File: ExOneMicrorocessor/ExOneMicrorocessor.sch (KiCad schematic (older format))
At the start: 15 parts, among them IC1 STM32G041C8T6, IC2 FT230XS, IC3 TLV73333PQDBVRQ1, J1 UJ2-MBH-3-SMT, J2 Conn_01x02, Y1 32.768 kHz, Y2 8 MHz

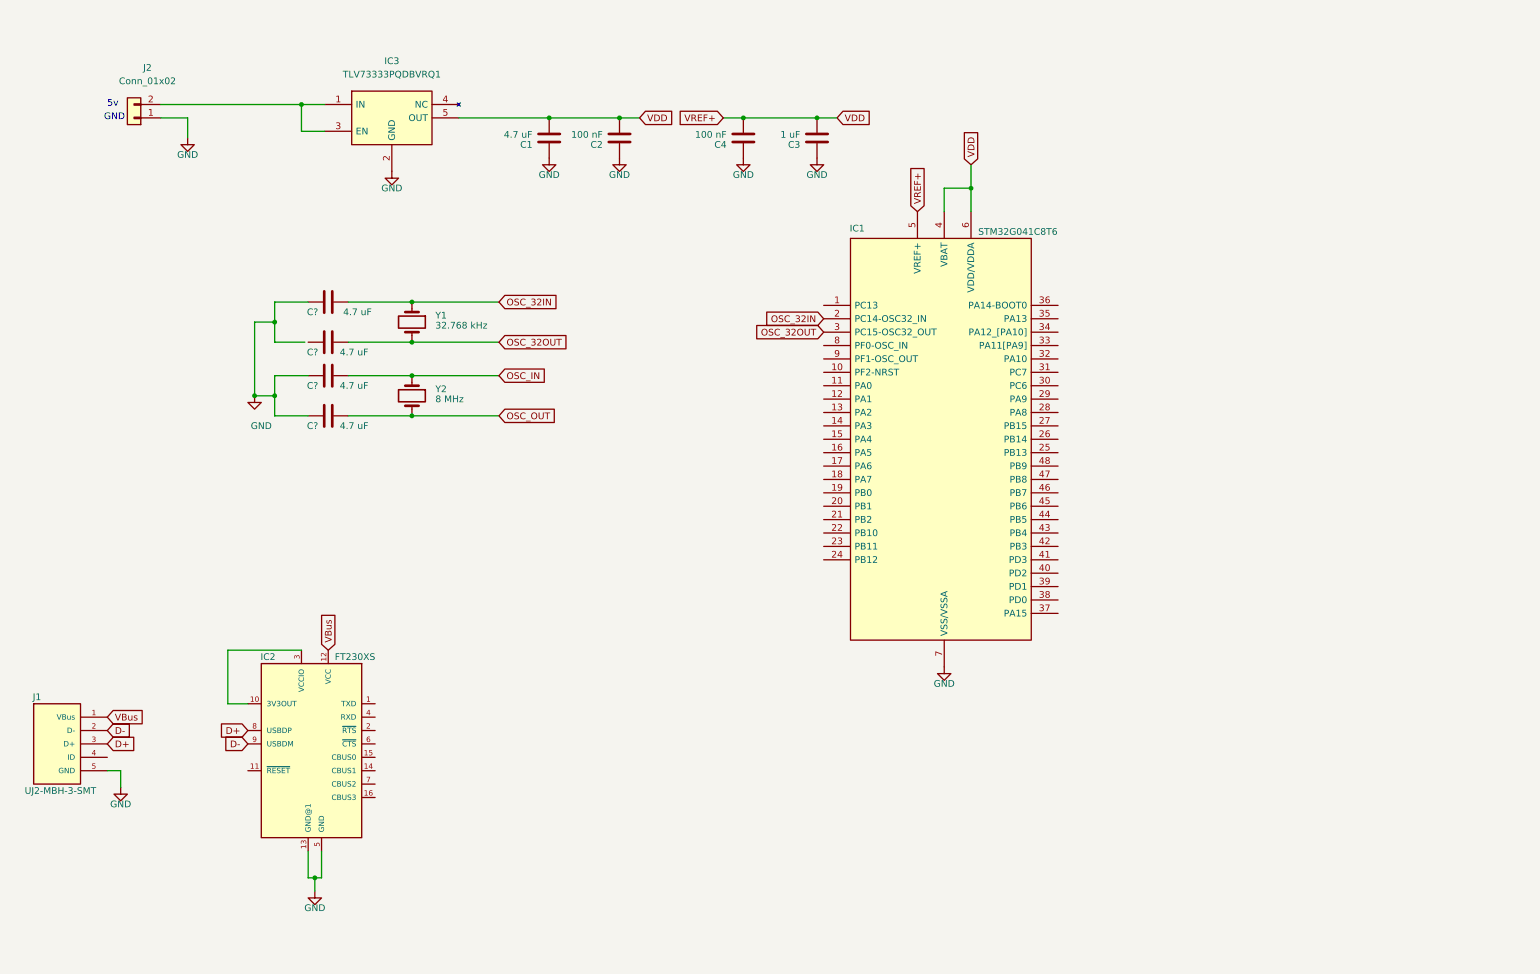
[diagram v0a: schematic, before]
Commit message: finished the schematic for the microP
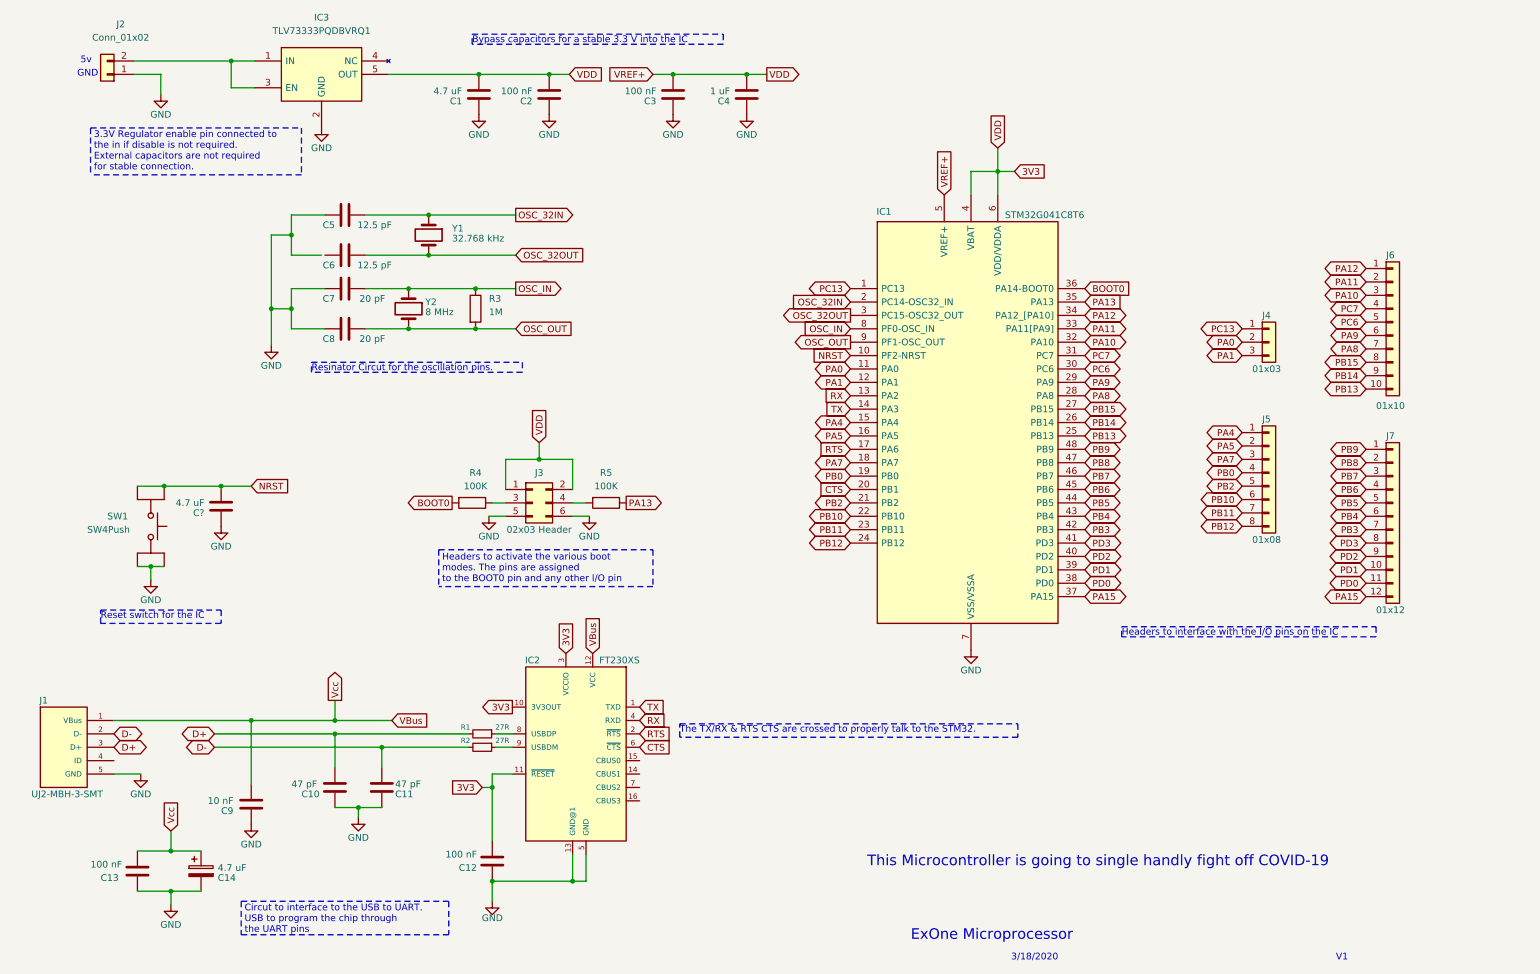
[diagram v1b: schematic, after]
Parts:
- added C10, C11: 47 pF, symbol Device:C
- added C12, C13: 100 nF, symbol Device:C
- added C14: 4.7 uF, symbol Device:CP
- added C9: 10 nF, symbol Device:C
- added C?: 4.7 uF, symbol Device:C
- added J3: 02x03 Header, symbol Connector_Generic:Conn_02x03_Odd_Even
- added J4: 01x03, symbol Connector_Generic:Conn_01x03
- added J5: 01x08, symbol Connector_Generic:Conn_01x08
- added J6: 01x10, symbol Connector_Generic:Conn_01x10
- added J7: 01x12, symbol Connector_Generic:Conn_01x12
- added R1, R2: 27R, symbol Device:R_Small
- added R3: 1M, symbol Device:R
- added R4, R5: 100K, symbol Device:R
- added SW1: SW4Push, symbol Switch4Prong:SW4Push
- C5, C6: renamed from C?; value 4.7 uF -> 12.5 pF
- C7, C8: renamed from C?; value 4.7 uF -> 20 pF
- renumbered C4 to C3, C3 to C4
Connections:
- net VDD is gone; now on net 3V3: C1.2, C2.2, C3.2, C4.2, IC1.4 (VBAT), IC1.5 (VREF+), IC1.6 (VDD/VDDA), IC3.5 (OUT)
- net D+: now also C10.1, R1.2; no longer IC2.8 (USBDP)
- net D-: now also C11.1, R2.2; no longer IC2.9 (USBDM)
- net GND: now also C10.2, C11.2, C12.2, C13.2, C14.2, C9.2, C?.1, J3.5 (Pin_5), J3.6 (Pin_6), SW1.1, SW1.4
- net OSC_IN: now also IC1.8 (PF0-OSC_IN), R3.1
- net OSC_OUT: now also IC1.9 (PF1-OSC_OUT), R3.2
- net VBus: now also C13.1, C14.1, C9.1
- net PC13: now reaches IC1.1 (PC13)
- net PC13: now also J4.1 (Pin_1)
- net NRST: now reaches IC1.10 (PF2-NRST)
- net NRST: now also C?.2, SW1.2, SW1.3
- net PA0: now reaches IC1.11 (PA0)
- net PA0: now also J4.2 (Pin_2)
- net PA1: now reaches IC1.12 (PA1)
- net PA1: now also J4.3 (Pin_3)
- net RX: now reaches IC1.13 (PA2)
- net RX: now also IC2.4 (RXD)
- net TX: now reaches IC1.14 (PA3)
- net TX: now also IC2.1 (TXD)
- net PA4: now reaches IC1.15 (PA4)
- net PA4: now also J5.1 (Pin_1)
- net PA5: now reaches IC1.16 (PA5)
- net PA5: now also J5.2 (Pin_2)
- net RTS: now reaches IC1.17 (PA6)
- net RTS: now also IC2.2 (~RTS~)
- net PA7: now reaches IC1.18 (PA7)
- net PA7: now also J5.3 (Pin_3)
- net PB0: now reaches IC1.19 (PB0)
- net PB0: now also J5.4 (Pin_4)
- net CTS: now reaches IC1.20 (PB1)
- net CTS: now also IC2.6 (~CTS~)
- net PB2: now reaches IC1.21 (PB2)
- net PB2: now also J5.5 (Pin_5)
- net PB10: now reaches IC1.22 (PB10)
- net PB10: now also J5.6 (Pin_6)
- net PB11: now reaches IC1.23 (PB11)
- net PB11: now also J5.7 (Pin_7)
- net PB12: now reaches IC1.24 (PB12)
- net PB12: now also J5.8 (Pin_8)
- net PB13: now reaches IC1.25 (PB13)
- net PB13: now also J6.10 (Pin_10)
- net PB14: now reaches IC1.26 (PB14)
- net PB14: now also J6.9 (Pin_9)
- net PB15: now reaches IC1.27 (PB15)
- net PB15: now also J6.8 (Pin_8)
- net PA8: now reaches IC1.28 (PA8)
- net PA8: now also J6.7 (Pin_7)
- net PA9: now reaches IC1.29 (PA9)
- net PA9: now also J6.6 (Pin_6)
- net PC6: now reaches IC1.30 (PC6)
- net PC6: now also J6.5 (Pin_5)
- net PC7: now reaches IC1.31 (PC7)
- net PC7: now also J6.4 (Pin_4)
- net PA10: now reaches IC1.32 (PA10)
- net PA10: now also J6.3 (Pin_3)
- net PA11: now reaches IC1.33 (PA11[PA9])
- net PA11: now also J6.2 (Pin_2)
- net PA12: now reaches IC1.34 (PA12_[PA10])
- net PA12: now also J6.1 (Pin_1)
- net PA13: now reaches IC1.35 (PA13)
- net PA13: now also R5.1
- net BOOT0: now reaches IC1.36 (PA14-BOOT0)
- net BOOT0: now also R4.2
- net PA15: now reaches IC1.37 (PA15)
- net PA15: now also J7.12 (Pin_12)
- net PD0: now reaches IC1.38 (PD0)
- net PD0: now also J7.11 (Pin_11)
- net PD1: now reaches IC1.39 (PD1)
- net PD1: now also J7.10 (Pin_10)
- net PD2: now reaches IC1.40 (PD2)
- net PD2: now also J7.9 (Pin_9)
- net PD3: now reaches IC1.41 (PD3)
- net PD3: now also J7.8 (Pin_8)
- net PB3: now reaches IC1.42 (PB3)
- net PB3: now also J7.7 (Pin_7)
- net PB4: now reaches IC1.43 (PB4)
- net PB4: now also J7.6 (Pin_6)
- net PB5: now reaches IC1.44 (PB5)
- net PB5: now also J7.5 (Pin_5)
- net PB6: now reaches IC1.45 (PB6)
- net PB6: now also J7.4 (Pin_4)
- net PB7: now reaches IC1.46 (PB7)
- net PB7: now also J7.3 (Pin_3)
- net PB8: now reaches IC1.47 (PB8)
- net PB8: now also J7.2 (Pin_2)
- net PB9: now reaches IC1.48 (PB9)
- net PB9: now also J7.1 (Pin_1)
- net 3V3: now reaches IC2.10 (3V3OUT), IC2.3 (VCCIO)
- net 3V3: now also IC2.11 (~RESET~), C12.1, J3.1 (Pin_1), J3.2 (Pin_2)
- new net: IC2.8 (USBDP), R1.1
- new net: IC2.9 (USBDM), R2.1
- new net: J3.3 (Pin_3), R4.1
- new net: J3.4 (Pin_4), R5.2
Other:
- note added: "3.3V Regulator enable pin connected to \nthe in if disable is not required.\nExternal capacitors are not required\nfor stable connection."
- note added: "3/18/2020"
- note added: "Bypass capacitors for a stable 3.3 V into the IC"
- note added: "Circut to interface to the USB to UART. \nUSB to program the chip through\nthe UART pins \n\n"
- note added: "ExOne Microprocessor"
- note added: "Headers to activate the various boot\nmodes. The pins are assigned \nto the BOOT0 pin and any other I/O pin"
- note added: "Headers to interface with the I/O pins on the IC"
- note added: "Reset switch for the IC"
- note added: "Resinator Circut for the oscillation pins."
- note added: "The TX/RX & RTS CTS are crossed to properly talk to the STM32."
- note added: "This Microcontroller is going to single handly fight off COVID-19"
- note added: "V1"
- moved on the sheet: C1, C2, C3, C4, C5, C6, C7, C8, IC1, IC2, IC3, J1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
